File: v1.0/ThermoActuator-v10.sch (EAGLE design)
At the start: 18 parts

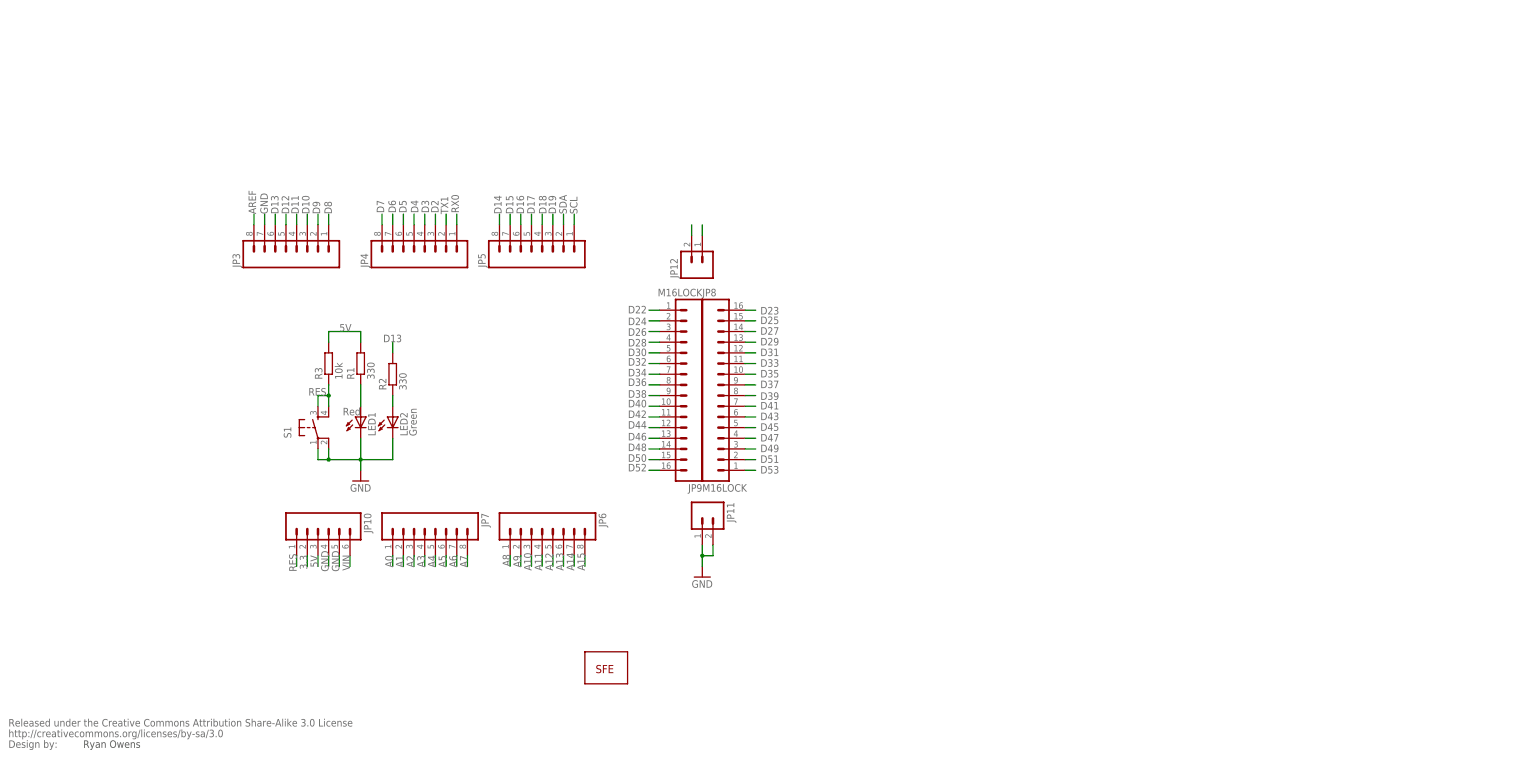
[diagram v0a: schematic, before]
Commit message: one thermistor ch laid out
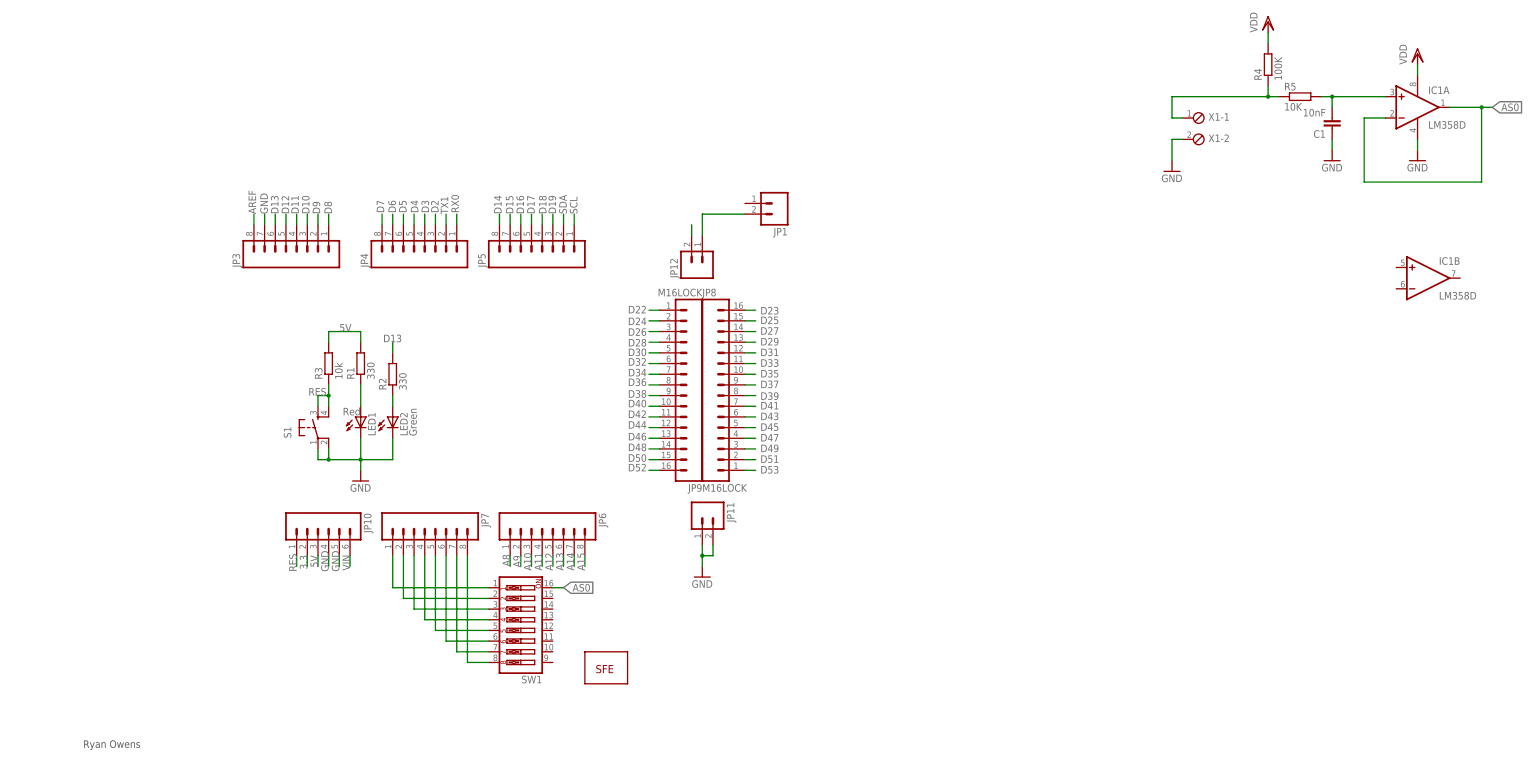
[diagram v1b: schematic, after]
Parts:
- removed U$2: CREATIVE_COMMONS, SparkFun:CREATIVE_COMMONS
- added C1: 10nF, rcl:C-EUC1206
- added IC1: LM358D, linear:LM358D
- added JP1: (no value), SparkFun:M02LOCK
- added R4: 100K, rcl:R-EU_R0805
- added R5: 10K, rcl:R-EU_R1206
- added SW1: (no value), special:SW_DIP-8
- added X1: (no value), con-phoenix-254:MPT2
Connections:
- removed net 5V@1: JP12.1, JP12.2
- removed net A0: JP7.1
- removed net A1: JP7.2
- removed net A2: JP7.3
- removed net A3: JP7.4
- removed net A4: JP7.5
- removed net A5: JP7.6
- removed net A6: JP7.7
- removed net A7: JP7.8
- new net AS0: IC1A.-IN, IC1A.OUT, SW1.16
- new net N$1: R4.1, R5.1, X1-1.1
- new net N$10: JP7.8, SW1.8
- new net N$2: C1.2, IC1A.+IN, R5.2
- new net N$3: JP7.1, SW1.1
- new net N$4: JP7.2, SW1.2
- new net N$5: JP7.3, SW1.3
- new net N$6: JP7.4, SW1.4
- new net N$7: JP7.5, SW1.5
- new net N$8: JP7.6, SW1.6
- new net N$9: JP7.7, SW1.7
- new net VDD: IC1P.V+, JP1.2, JP12.1, JP12.2, R4.2
- net GND: now also C1.1, IC1P.V-, X1-2.1

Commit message: two channels laid out
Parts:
- added C2: 10nF, rcl:C-EUC1206
- added R6: 100K, rcl:R-EU_R0805
- added R7: 10K, rcl:R-EU_R1206
- added X2: (no value), con-phoenix-254:MPT2
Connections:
- new net AS1: IC1B.-IN, IC1B.OUT, SW1.15
- new net N$11: R6.1, R7.1, X2-1.1
- new net N$12: C2.2, IC1B.+IN, R7.2
- net GND: now also C2.1, X2-2.1
- net VDD: now also R6.2
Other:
- moved on the sheet: IC1B
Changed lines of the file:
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@@
 <part name="SW1" library="special" deviceset="SW_DIP-8" device=""/>
 <part name="JP1" library="SparkFun" deviceset="M02" device="LOCK"/>
+<part name="X2" library="con-phoenix-254" deviceset="MPT2" device=""/>
+<part name="GND6" library="supply1" deviceset="GND" device=""/>
+<part name="GND7" library="supply1" deviceset="GND" device=""/>
+<part name="R6" library="rcl" deviceset="R-EU_" device="R0805" value="100K"/>
+<part name="VDD3" library="supply1" deviceset="VDD" device=""/>
+<part name="R7" library="rcl" deviceset="R-EU_" device="R1206" value="10K"/>
+<part name="C2" library="rcl" deviceset="C-EU" device="C1206" value="10nF"/>
+<part name="GND8" library="supply1" deviceset="GND" device=""/>
 </parts>
 <sheets>
@@
 <instance part="X1" gate="-2" x="294.64" y="154.94"/>
 <instance part="IC1" gate="A" x="347.98" y="162.56"/>
-<instance part="IC1" gate="B" x="350.52" y="121.92"/>
+<instance part="IC1" gate="B" x="350.52" y="114.3"/>
 <instance part="R4" gate="G$1" x="312.42" y="172.72" rot="R90"/>
 <instance part="R5" gate="G$1" x="320.04" y="165.1"/>
@@
 <instance part="SW1" gate="A" x="134.62" y="38.1" rot="R180"/>
 <instance part="JP1" gate="G$1" x="195.58" y="139.7" rot="R180"/>
+<instance part="X2" gate="-1" x="294.64" y="109.22"/>
+<instance part="X2" gate="-2" x="294.64" y="104.14"/>
+<instance part="GND6" gate="1" x="289.56" y="147.32"/>
+<instance part="GND7" gate="1" x="289.56" y="96.52"/>
+<instance part="R6" gate="G$1" x="312.42" y="124.46" rot="R90"/>
+<instance part="VDD3" gate="G$1" x="312.42" y="134.62"/>
+<instance part="R7" gate="G$1" x="320.04" y="116.84"/>
+<instance part="C2" gate="G$1" x="330.2" y="109.22" rot="R180"/>
+<instance part="GND8" gate="1" x="330.2" y="101.6"/>
 </instances>
 <busses>
@@
 <pinref part="X1" gate="-2" pin="1"/>
 <wire x1="289.56" y1="154.94" x2="292.1" y2="154.94" width="0.1524" layer="91"/>
+<pinref part="GND6" gate="1" pin="GND"/>
+<junction x="289.56" y="149.86"/>
 </segment>
 <segment>
@@
 <pinref part="IC1" gate="P" pin="V-"/>
 <wire x1="347.98" y1="152.4" x2="347.98" y2="154.94" width="0.1524" layer="91"/>
+</segment>
+<segment>
+<pinref part="GND7" gate="1" pin="GND"/>
+<wire x1="289.56" y1="99.06" x2="289.56" y2="104.14" width="0.1524" layer="91"/>
+<pinref part="X2" gate="-2" pin="1"/>
+<wire x1="289.56" y1="104.14" x2="292.1" y2="104.14" width="0.1524" layer="91"/>
+</segment>
+<segment>
+<pinref part="GND8" gate="1" pin="GND"/>
+<pinref part="C2" gate="G$1" pin="1"/>
+<wire x1="330.2" y1="104.14" x2="330.2" y2="106.68" width="0.1524" layer="91"/>
 </segment>
 </net>
@@
 <pinref part="JP1" gate="G$1" pin="2"/>
 <wire x1="177.8" y1="137.16" x2="187.96" y2="137.16" width="0.1524" layer="91"/>
+</segment>
+<segment>
+<pinref part="R6" gate="G$1" pin="2"/>
+<pinref part="VDD3" gate="G$1" pin="VDD"/>
+<wire x1="312.42" y1="129.54" x2="312.42" y2="132.08" width="0.1524" layer="91"/>
 </segment>
 </net>
@@
 </segment>
 </net>
+<net name="N$11" class="0">
+<segment>
+<pinref part="X2" gate="-1" pin="1"/>
+<wire x1="292.1" y1="109.22" x2="289.56" y2="109.22" width="0.1524" layer="91"/>
+<wire x1="289.56" y1="109.22" x2="289.56" y2="116.84" width="0.1524" layer="91"/>
+<pinref part="R7" gate="G$1" pin="1"/>
+<wire x1="289.56" y1="116.84" x2="312.42" y2="116.84" width="0.1524" layer="91"/>
+<pinref part="R6" gate="G$1" pin="1"/>
+<wire x1="312.42" y1="116.84" x2="314.96" y2="116.84" width="0.1524" layer="91"/>
+<wire x1="312.42" y1="119.38" x2="312.42" y2="116.84" width="0.1524" layer="91"/>
+<junction x="312.42" y="116.84"/>
+</segment>
+</net>
+<net name="N$12" class="0">
+<segment>
+<pinref part="R7" gate="G$1" pin="2"/>
+<pinref part="IC1" gate="B" pin="+IN"/>
+<wire x1="325.12" y1="116.84" x2="330.2" y2="116.84" width="0.1524" layer="91"/>
+<pinref part="C2" gate="G$1" pin="2"/>
+<wire x1="330.2" y1="116.84" x2="342.9" y2="116.84" width="0.1524" layer="91"/>
+<wire x1="330.2" y1="114.3" x2="330.2" y2="116.84" width="0.1524" layer="91"/>
+<junction x="330.2" y="116.84"/>
+</segment>
+</net>
+<net name="AS1" class="0">
+<segment>
+<pinref part="IC1" gate="B" pin="-IN"/>
+<wire x1="342.9" y1="111.76" x2="340.36" y2="111.76" width="0.1524" layer="91"/>
+<wire x1="340.36" y1="111.76" x2="340.36" y2="101.6" width="0.1524" layer="91"/>
+<wire x1="340.36" y1="101.6" x2="363.22" y2="101.6" width="0.1524" layer="91"/>
+<wire x1="363.22" y1="101.6" x2="363.22" y2="114.3" width="0.1524" layer="91"/>
+<pinref part="IC1" gate="B" pin="OUT"/>
+<wire x1="363.22" y1="114.3" x2="358.14" y2="114.3" width="0.1524" layer="91"/>
+<wire x1="363.22" y1="114.3" x2="365.76" y2="114.3" width="0.1524" layer="91"/>
+<junction x="363.22" y="114.3"/>
+<label x="365.76" y="114.3" size="1.778" layer="95" xref="yes"/>
+</segment>
+<segment>
+<pinref part="SW1" gate="A" pin="15"/>
+<wire x1="142.24" y1="45.72" x2="144.78" y2="45.72" width="0.1524" layer="91"/>
+<label x="144.78" y="45.72" size="1.778" layer="95" xref="yes"/>
+</segment>
+</net>

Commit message: centered with the right edge untouched
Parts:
- removed U$1: LOGO-SFENEW, SparkFun:LOGO-SFENEW
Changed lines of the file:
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@@
 <parts>
 <part name="FRAME1" library="SparkFun" deviceset="FRAME-LETTER" device=""/>
-<part name="U$1" library="SparkFun" deviceset="LOGO-SFE" device="NEW"/>
 <part name="JP3" library="SparkFun" deviceset="M08" device="LOCK"/>
 <part name="JP4" library="SparkFun" deviceset="M08" device="LOCK"/>
@@
 <instance part="FRAME1" gate="G$1" x="0" y="0"/>
 <instance part="FRAME1" gate="G$2" x="147.32" y="0"/>
-<instance part="U$1" gate="G$1" x="152.4" y="27.94"/>
 <instance part="JP3" gate="G$1" x="81.28" y="129.54" rot="R90"/>
 <instance part="JP4" gate="G$1" x="111.76" y="129.54" rot="R90"/>

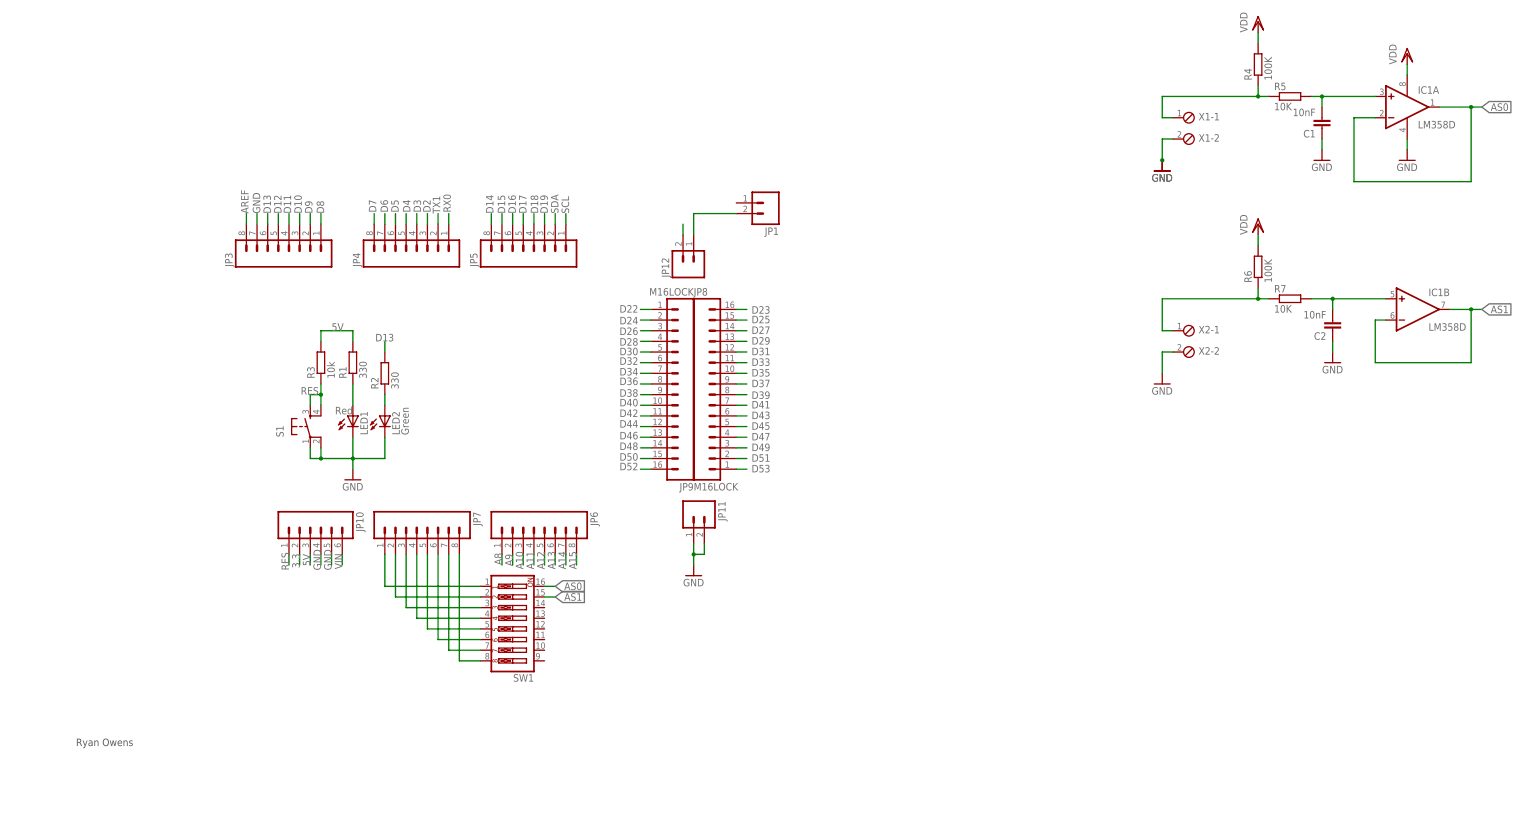
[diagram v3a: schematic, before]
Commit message: 4 ADC channels and 8 actuators
somewhat messy, 20 vias. The sparkfun's recommended drc used
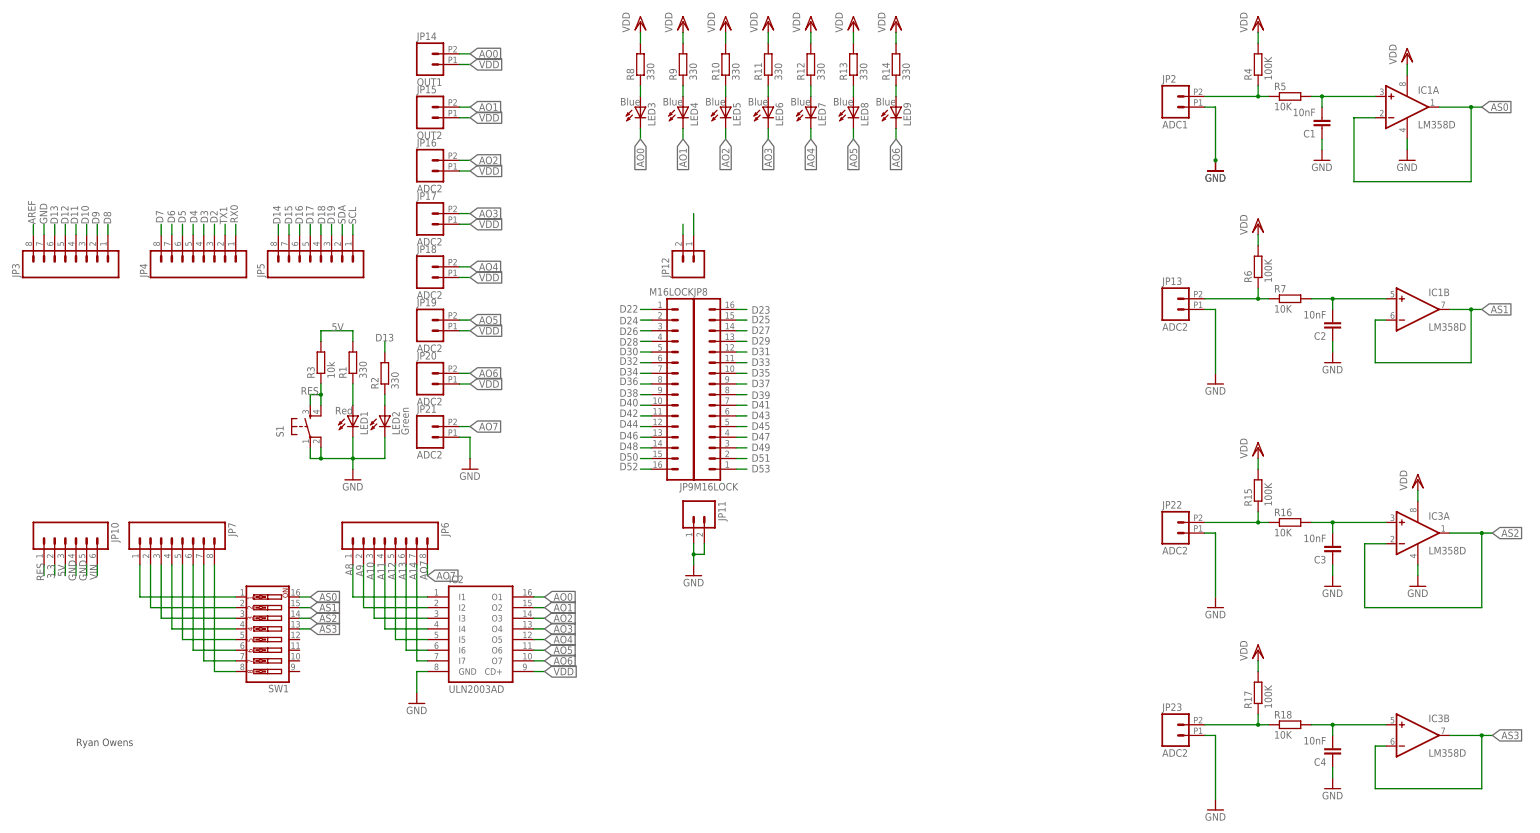
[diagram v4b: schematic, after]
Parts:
- removed JP1: (no value), SparkFun:M02LOCK
- removed X1, X2: (no value), con-phoenix-254:MPT2
- added C3, C4: 10nF, rcl:C-EUC1206
- added IC2: ULN2003AD, uln-udn:ULN2003AD
- added IC3: LM358D, linear:LM358D
- added JP13, JP16, JP17, JP18, JP19, JP20, JP21, JP22, JP23: ADC2, SparkFun-Connectors:M022.54MM_SCREWTERM
- added JP14: OUT1, SparkFun-Connectors:M022.54MM_SCREWTERM
- added JP15: OUT2, SparkFun-Connectors:M022.54MM_SCREWTERM
- added JP2: ADC1, SparkFun-Connectors:M022.54MM_SCREWTERM
- added LED3, LED4, LED5, LED6, LED7, LED8, LED9: Blue, led:LEDCHIP-LED0805
- added R10, R11, R12, R13, R14, R8, R9: 330, rcl:R-EU_R0805
- added R15, R17: 100K, rcl:R-EU_R0805
- added R16, R18: 10K, rcl:R-EU_R1206
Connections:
- removed net A15: JP6.8
- new net AO0: IC2.O1, JP14.2, LED3.C
- new net AO1: IC2.O2, JP15.2, LED4.C
- new net AO2: IC2.O3, JP16.2, LED5.C
- new net AO3: IC2.O4, JP17.2, LED6.C
- new net AO4: IC2.O5, JP18.2, LED7.C
- new net AO5: IC2.O6, JP19.2, LED8.C
- new net AO6: IC2.O7, JP20.2, LED9.C
- new net AO7: JP21.2, JP6.8
- new net AS2: IC3A.-IN, IC3A.OUT, SW1.14
- new net AS3: IC3B.-IN, IC3B.OUT, SW1.13
- new net N$13: LED3.A, R8.1
- new net N$14: LED4.A, R9.1
- new net N$15: LED5.A, R10.1
- new net N$16: LED6.A, R11.1
- new net N$17: LED7.A, R12.1
- new net N$18: LED8.A, R13.1
- new net N$19: LED9.A, R14.1
- new net N$20: JP22.2, R15.1, R16.1
- new net N$21: C3.2, IC3A.+IN, R16.2
- new net N$22: JP23.2, R17.1, R18.1
- new net N$23: C4.2, IC3B.+IN, R18.2
- net A10: now also IC2.I3
- net A11: now also IC2.I4
- net A12: now also IC2.I5
- net A13: now also IC2.I6
- net A14: now also IC2.I7
- net A8: now also IC2.I1
- net A9: now also IC2.I2
- net GND: now also C3.1, C4.1, IC2.GND, IC3P.V-, JP13.1, JP2.1, JP21.1, JP22.1, JP23.1; no longer X1-2.1, X2-2.1
- net N$1: now also JP2.2; no longer X1-1.1
- net N$11: now also JP13.2; no longer X2-1.1
- net VDD: now also IC2.CD+, IC3P.V+, JP14.1, JP15.1, JP16.1, JP17.1, JP18.1, JP19.1, JP20.1, R10.2, R11.2, R12.2, R13.2, R14.2, R15.2, R17.2, R8.2, R9.2; no longer JP1.2
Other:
- moved on the sheet: JP10, JP3, JP4, JP5, JP6, JP7, SW1

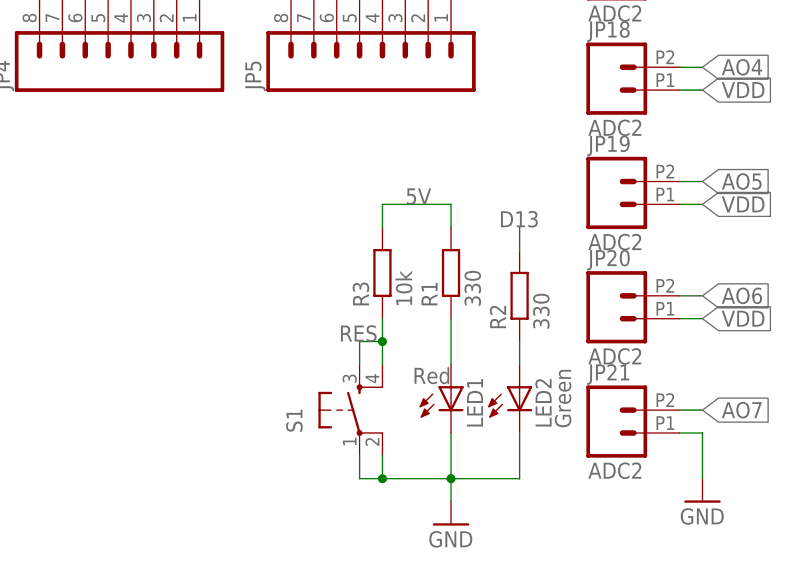
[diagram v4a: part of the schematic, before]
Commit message: down to 126 DRC errors
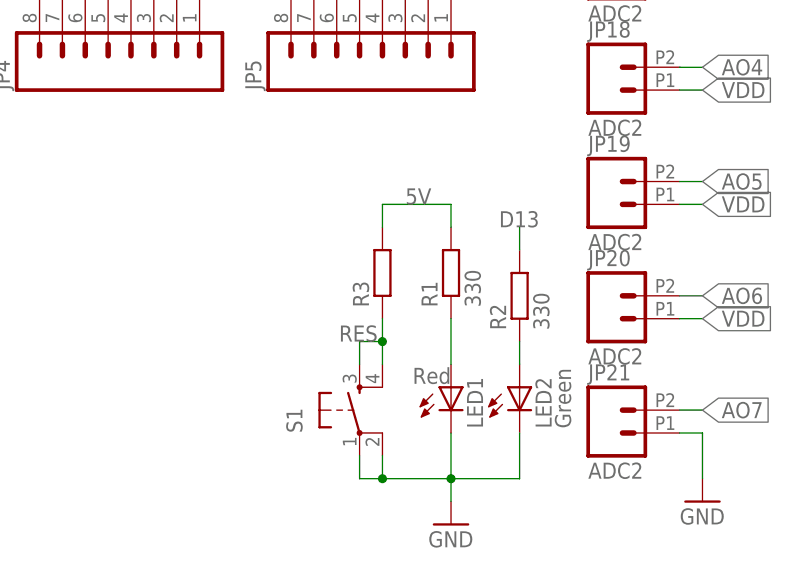
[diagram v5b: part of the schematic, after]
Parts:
- R3: value 10k -> (none)
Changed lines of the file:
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@@
 <part name="R1" library="rcl" deviceset="R-EU_" device="R0805" value="330"/>
 <part name="R2" library="rcl" deviceset="R-EU_" device="R0805" value="330"/>
-<part name="R3" library="rcl" deviceset="R-EU_" device="R0805" value="10k"/>
+<part name="R3" library="rcl" deviceset="R-EU_" device="R0805"/>
 <part name="GND1" library="SparkFun" deviceset="GND" device=""/>
 <part name="GND2" library="SparkFun" deviceset="GND" device=""/>
